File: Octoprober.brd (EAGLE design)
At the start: 100 x 80 mm, 98 parts, among them J1 10118193-0001LF, P1 TC33X-1, SW1 EVQ-Q2203W, SW2 EVQ-Q2203W, SW3 EVQ-Q2203W, SW4 EVQ-Q2203W, SW5 EVQ-Q2203W, U1 P8X32A-M44, U10 MAX31855KASA+, U11 MAX31855KASA+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

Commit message: Worked on the layout some more.
Still need lots of work and connectors.
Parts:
- U1: device PP_DigitalIC:DUAL_LQFP_QFN_44 -> PP_DigitalIC:QFN-44
- moved R1 235.2 mm to (126.1, 54.2), turned to 90 degrees
- moved R2 235.1 mm to (113.3, 24.9), turned to 90 degrees
- moved C6 235.1 mm to (121.4, 32.5)
- moved C4 224.7 mm to (124.1, 54.2), turned to 270 degrees
- moved C5 219.5 mm to (116.3, 60.8)
- moved C1 218.4 mm to (120.1, 24.9), turned to 90 degrees
- moved C3 215.6 mm to (117.0, 47.8), turned to 180 degrees
- moved R27 210.7 mm to (81.5, 17.0), turned to 270 degrees
- moved R26 209.2 mm to (83.7, 17.0), turned to 270 degrees
- moved C2 203.3 mm to (109.3, 52.7), turned to 180 degrees
- moved R23 201.0 mm to (96.5, 40.6)
- moved SW2 200.8 mm to (96.5, 61.2)
- moved R22 193.2 mm to (96.5, 53.3)
- moved C35 192.7 mm to (72.4, 20.1), turned to 270 degrees
- moved D2 188.4 mm to (107.7, 86.6), turned to 90 degrees
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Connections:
- removed net P26: U1.33, U1.77
- removed net SD_CLK: U1.43, U1.87
- net !SLEEP: no longer U1.67
- net 3.3V: no longer U1.52, U1.62, U1.74, U1.84
- net BK_GATE: no longer U1.68
- net CHARGING: no longer U1.66
- net GND: no longer U1.49, U1.50, U1.61, U1.71, U1.83, U1.PAD
- net LCD_D4: now also U1.9; no longer U1.2, U1.46
- net LCD_D5: now also U1.4; no longer U1.3, U1.47
- net LCD_D6: now also U1.3; no longer U1.4, U1.48
- net LCD_D7: now also U1.2; no longer U1.53, U1.9
- net LCD_E: now also U1.33
- net LCD_RS: no longer U1.45
- net P27: no longer U1.78
- net PWR_SW: no longer U1.76
- net RES: no longer U1.51
- net RX: no longer U1.81
- net SCL: no longer U1.79
- net SDA: no longer U1.80
- net SD_CS: now also U1.44; no longer U1.41, U1.85
- net SD_DI: now also U1.43; no longer U1.42, U1.86
- net SD_DO: now also U1.41; no longer U1.44, U1.88
- net SD_SCLK: now also U1.42
- net SW_DWN: no longer U1.75
- net SW_SEL: no longer U1.70
- net SW_UP: no longer U1.69
- net TP_CS0: no longer U1.56
- net TP_CS1: no longer U1.57
- net TP_CS2: no longer U1.58
- net TP_CS3: no longer U1.59
- net TP_CS4: no longer U1.60
- net TP_CS5: no longer U1.63
- net TP_CS6: no longer U1.64
- net TP_CS7: no longer U1.65
- net TP_SCK: now also U1.10; no longer U1.11, U1.55
- net TP_SO: now also U1.11; no longer U1.10, U1.54
- net TX: no longer U1.82
- net X0: no longer U1.73
- net X1: no longer U1.72
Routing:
- net GND: track 3.51 -> 272.1 mm, vias 0 -> 47
- net 3.3V: track 0.00 -> 154.6 mm, vias 0 -> 17
- net TP_SO: track 0.00 -> 154.4 mm, vias 0 -> 8
- net TP_SCK: track 0.00 -> 150.3 mm, vias 0 -> 9
- net TP_CS7: track 0.00 -> 117.4 mm
- net TP_CS6: track 0.00 -> 107.4 mm
- net TP_CS5: track 0.00 -> 97.7 mm
- net TP_CS4: track 0.00 -> 88.7 mm
- net TX: track 0.00 -> 82.3 mm
- net TP_CS3: track 0.00 -> 79.3 mm
- net RX: track 0.00 -> 73.4 mm
- net PWR_SW: track 0.00 -> 69.8 mm
- net TP_CS2: track 0.00 -> 69.7 mm
- net RES: track 0.00 -> 62.1 mm
- net BK_GATE: track 0.00 -> 61.4 mm
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- added copper zone on layer 15, net 3.3V
- added copper zone on layer 1, net GND
- added copper zone on layer 2, net GND
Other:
- board size 100 x 80 mm -> 71.6 x 26.4 mm

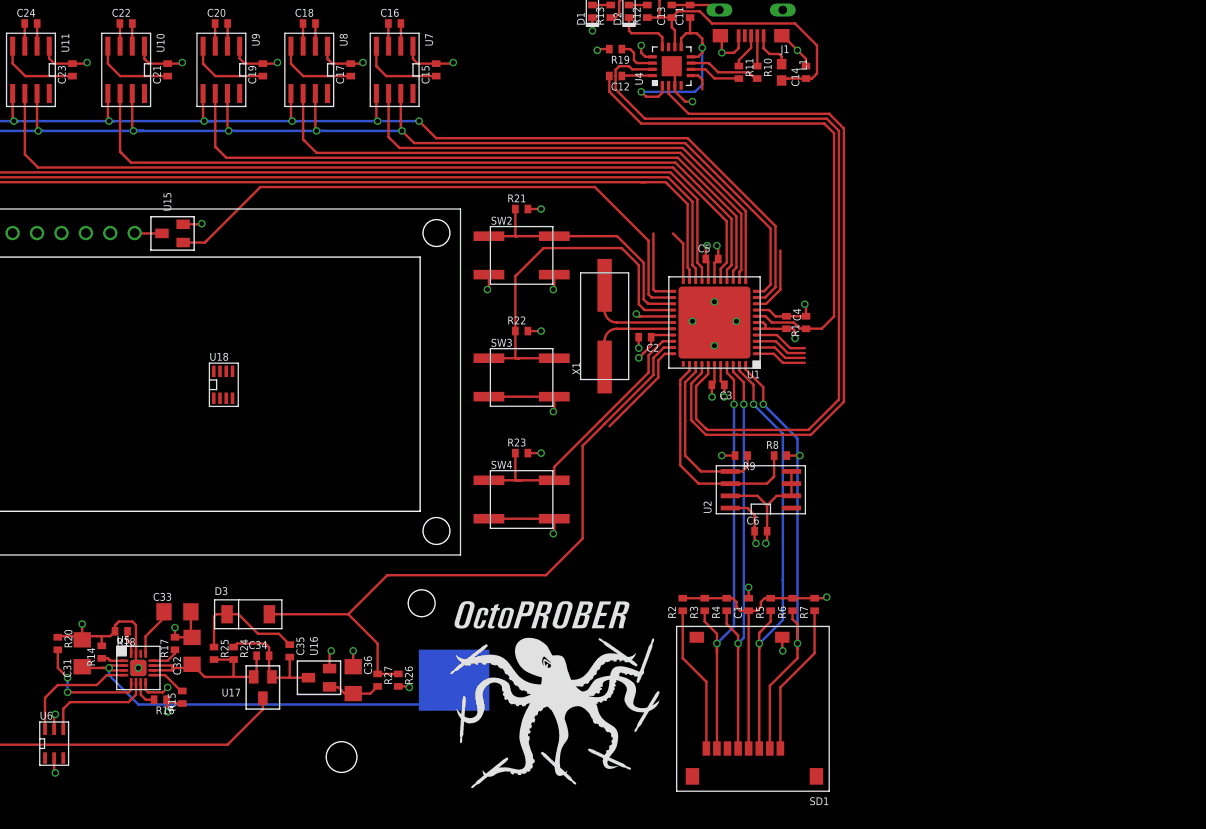
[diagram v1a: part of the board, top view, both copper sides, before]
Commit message: Add optocouple.
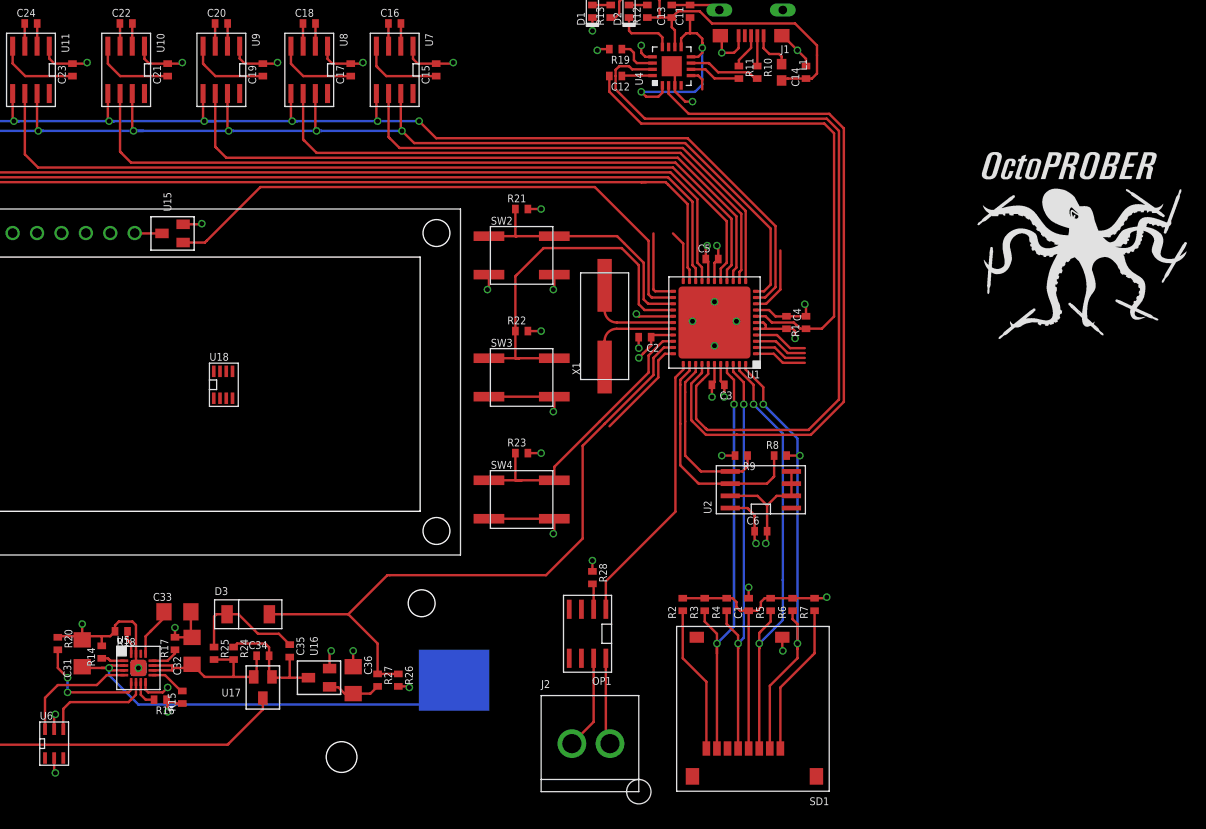
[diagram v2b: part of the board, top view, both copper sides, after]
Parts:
- added J2: 26-60-4020, PP_Connectors:MOLEX_KK_2
- added OP1: (no value), PP_DigitalIC:SOIC-8
- added R28: 120, PP_Passives:0402
- moved U$2 72.1 mm to (143.0, 52.3)
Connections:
- removed net P27: U1.34
- new net EXT: OP1.1, U1.34
- new net EXT_CON_0: J2.P$2, OP1.8
- new net EXT_CON_1: J2.P$1, OP1.7
- new net N$6: OP1.2, R28.2
- net GND: now also R28.1
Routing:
- net EXT: track 0.00 -> 28.9 mm
- net EXT_CON_1: track 0.00 -> 9.82 mm
- net EXT_CON_0: track 0.00 -> 9.06 mm
- net N$6: track 0.00 -> 2.69 mm
- net GND: track 272.1 -> 269.9 mm, vias 47 -> 48

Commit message: Finished preliminary routing
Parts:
- removed U18: AD7999YRJZ-1500RL7, PP_DigitalIC:SOT-23-8
- added TC1, TC2, TC3, TC4, TC5, TC6, TC7, TC8: (no value), PP_Connectors:HEADER_01X02_PTH
- SW1: value EVQ-Q2203W -> 101-0134-EV; device PP_Electromechanical:EVQ-Q2203W -> PP_Electromechanical:101-0134-EV
- moved U$2 152.6 mm to (-0.51, 0.51)
- moved SW1 101.4 mm to (99.3, 75.9)
- moved U$1 11.1 mm to (1.02, 20.8)
- moved LCD1 4.20 mm to (8.38, 62.2)
- moved R21 4.20 mm to (94.7, 62.2)
- moved C11 4.20 mm to (112.3, 82.8)
- moved C12 4.20 mm to (104.5, 76.1)
- moved C13 4.20 mm to (110.4, 82.8)
- moved C19 4.20 mm to (67.8, 76.7)
- moved C3 4.20 mm to (115.2, 43.9)
- moved D3 4.20 mm to (66.3, 20.1)
- moved OP1 4.20 mm to (101.6, 18.0)
- moved R1 4.20 mm to (124.3, 50.4)
- moved R12 4.20 mm to (107.8, 82.8)
- moved R19 4.20 mm to (104.5, 78.9)
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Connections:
- net GND: no longer SW1.2
- net RES: now also SW1.2; no longer SW1.3, SW1.4
- net TP_T+_0: now also TC1.2
- net TP_T+_1: now also TC2.2
- net TP_T+_2: now also TC3.2
- net TP_T+_3: now also TC4.2
- net TP_T+_4: now also TC5.2
- net TP_T+_5: now also TC6.2
- net TP_T+_6: now also TC7.2
- net TP_T+_7: now also TC8.2
- net TP_T-_0: now also TC1.1
- net TP_T-_1: now also TC2.1
- net TP_T-_2: now also TC3.1
- net TP_T-_3: now also TC4.1
- net TP_T-_4: now also TC5.1
- net TP_T-_5: now also TC6.1
- net TP_T-_6: now also TC7.1
- net TP_T-_7: now also TC8.1
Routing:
- net !PWREN: track 4.24 -> 200.1 mm, vias 0 -> 2
- net !SLEEP: track 7.97 -> 202.1 mm, vias 0 -> 3
- net USB_V1: track 44.0 -> 221.1 mm, vias 0 -> 2
- net BCD_CHARGER: track 14.7 -> 156.3 mm, vias 2 -> 3
- net LCD_RS: track 5.49 -> 130.2 mm, vias 0 -> 1
- net CHARGING: track 9.17 -> 117.9 mm, vias 0 -> 2
- net LCD_D5: track 5.66 -> 108.4 mm, vias 0 -> 1
- net LCD_D6: track 5.61 -> 102.1 mm, vias 0 -> 1
- net 3.3V: track 154.6 -> 250.1 mm, vias 17 -> 26
- net LCD_E: track 10.8 -> 103.1 mm, vias 0 -> 1
- net N$4: track 19.2 -> 110.6 mm
- net LCD_D7: track 5.55 -> 96.2 mm, vias 0 -> 1
- net LCD_D4: track 7.23 -> 94.8 mm, vias 0 -> 1
- net RES: track 62.1 -> 52.7 mm
- net TX: track 82.3 -> 74.3 mm
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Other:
- board size 71.6 x 26.4 mm -> 130.8 x 86.9 mm

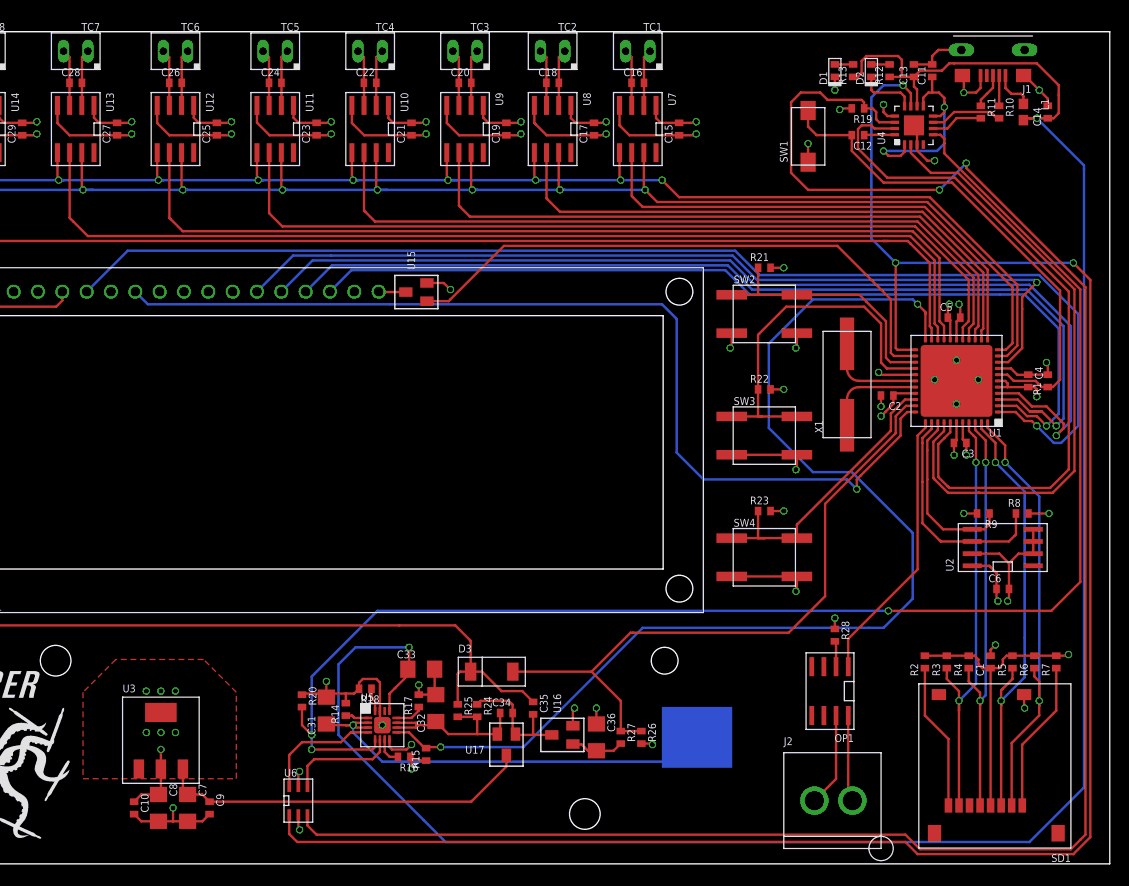
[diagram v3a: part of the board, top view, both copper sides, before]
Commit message: Added RTC.
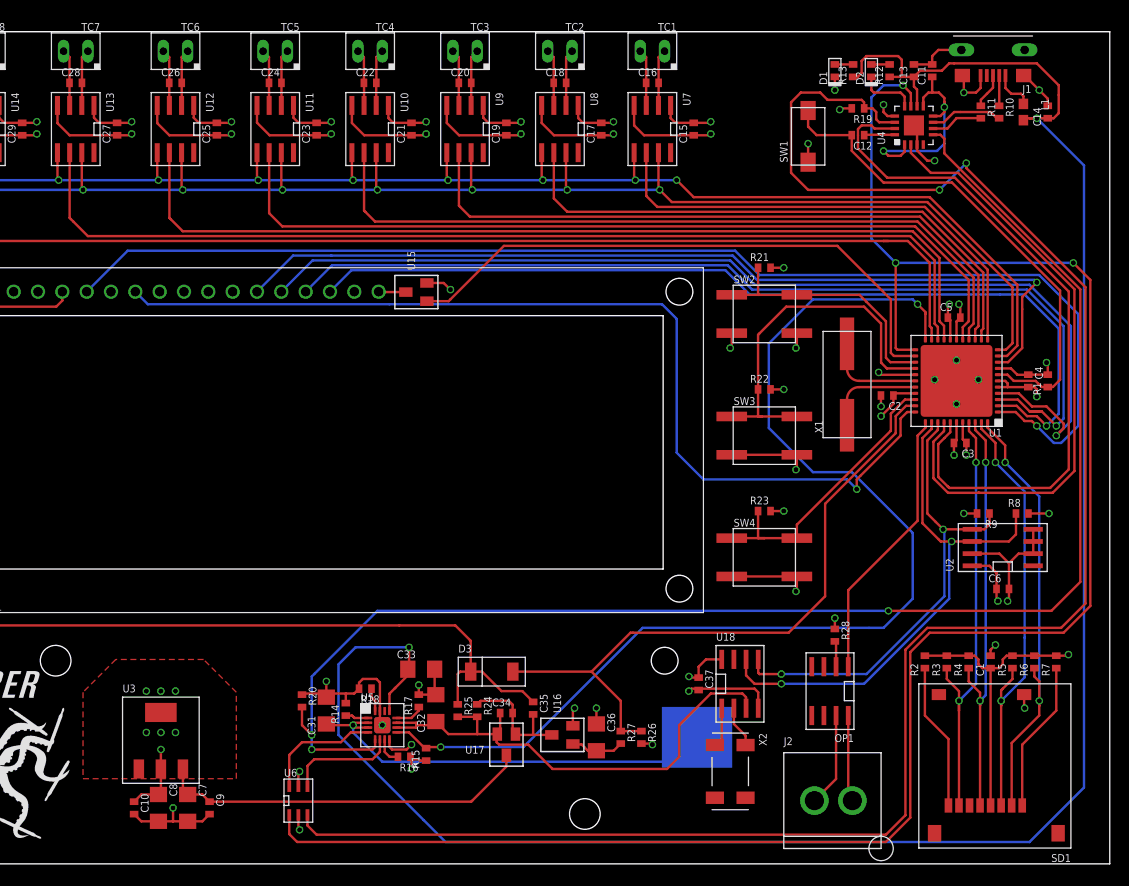
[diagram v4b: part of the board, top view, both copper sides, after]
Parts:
- added C37: 0.1uF, PP_Passives:0402
- added U18: DS1340Z-33+, PP_DigitalIC:SOIC-8
- added X2: ABS25-32.768KHz-1-T, PP_FreqCtrl:8MM_X_3.8MM
- moved C15 1.52 mm to (87.4, 76.7)
- moved C16 1.52 mm to (83.1, 81.5)
- moved TC1 1.52 mm to (84.3, 84.8)
- moved U7 1.52 mm to (83.1, 76.7)
- moved C17 0.76 mm to (77.7, 76.7)
- moved C18 0.76 mm to (73.4, 81.5)
- moved TC2 0.76 mm to (74.7, 84.8)
- moved U8 0.76 mm to (73.4, 76.7)
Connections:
- new net RTC_X1: U18.1, X2.1
- new net RTC_X2: U18.2, X2.4
- net 3.3V: now also C37.1, U18.8
- net GND: now also C37.2, U18.4
- net SCL: now also U18.6
- net SDA: now also U18.5
- net SYS_V: now also U18.3
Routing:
- net SYS_V: track 20.0 -> 54.6 mm
- net SCL: track 24.0 -> 57.0 mm, vias 0 -> 2
- net SDA: track 18.5 -> 49.8 mm, vias 0 -> 2
- net GND: track 273.2 -> 283.1 mm, vias 48 -> 49
- net !PWREN: track 200.1 -> 194.8 mm
- net !SLEEP: track 202.1 -> 197.1 mm
- net RTC_X1: track 0.00 -> 4.55 mm
- net RTC_X2: track 0.00 -> 4.35 mm
- net TP_SO: track 154.4 -> 150.3 mm
- net TP_SCK: track 150.3 -> 146.7 mm
- net 3.3V: track 250.1 -> 253.4 mm, vias 26 -> 27
- net TP_CS0: track 52.2 -> 50.7 mm
- net VBATT: track 46.2 -> 45.4 mm
- net TP_CS1: track 60.7 -> 59.9 mm
